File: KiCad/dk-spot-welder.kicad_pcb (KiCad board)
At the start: 4 copper layers, 112 x 72 mm, 49 parts, among them Q1 IRF1404, Q2 IRF1404, Q3 IRF1404, Q4 IRF1404, Q5 IRF1404, Q6 IRF1404, Q7 IRF1404, Q8 IRF1404, U1 MCP1407, U2 L7805, U3 ATtiny13-20P, U4 PC817

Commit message: added PCBWay logo
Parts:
- added G***: LOGO, LOGO, B.Cu at (107.5, 129.0)

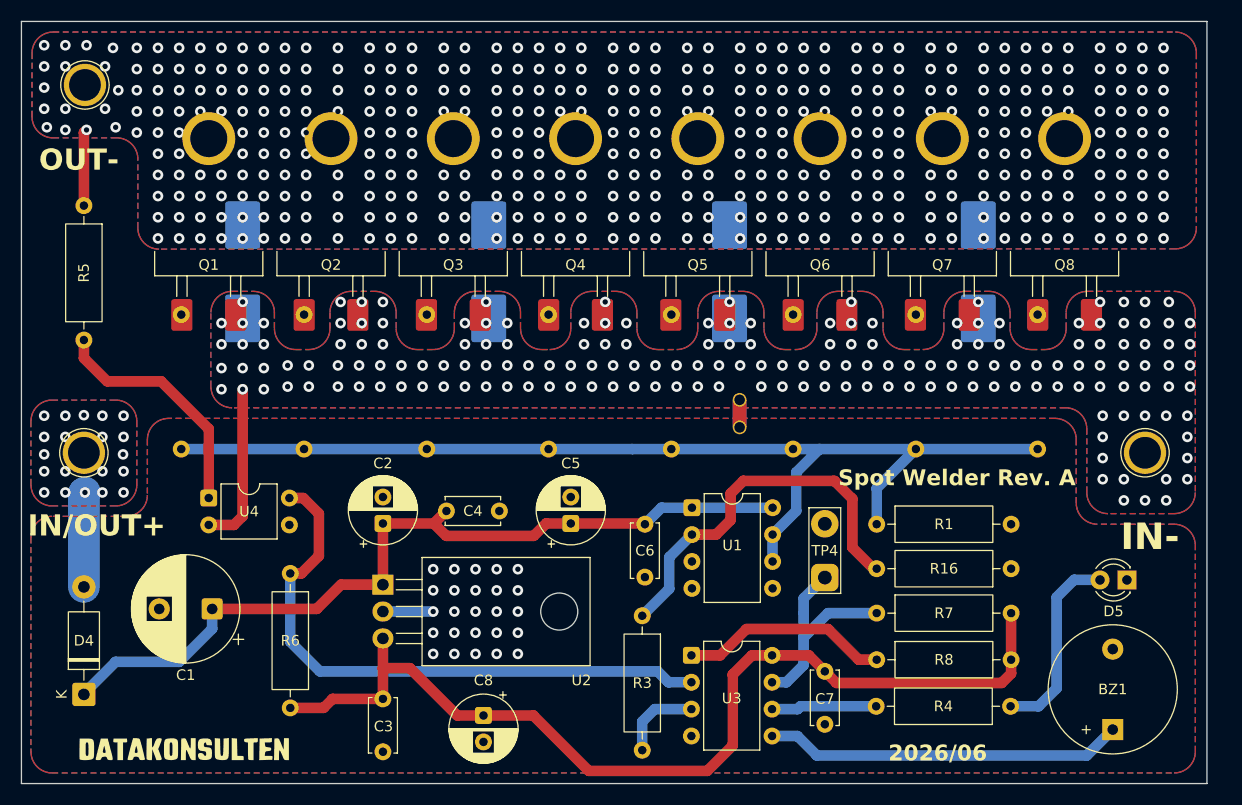
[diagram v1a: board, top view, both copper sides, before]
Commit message: update connections from M3 to 4mm
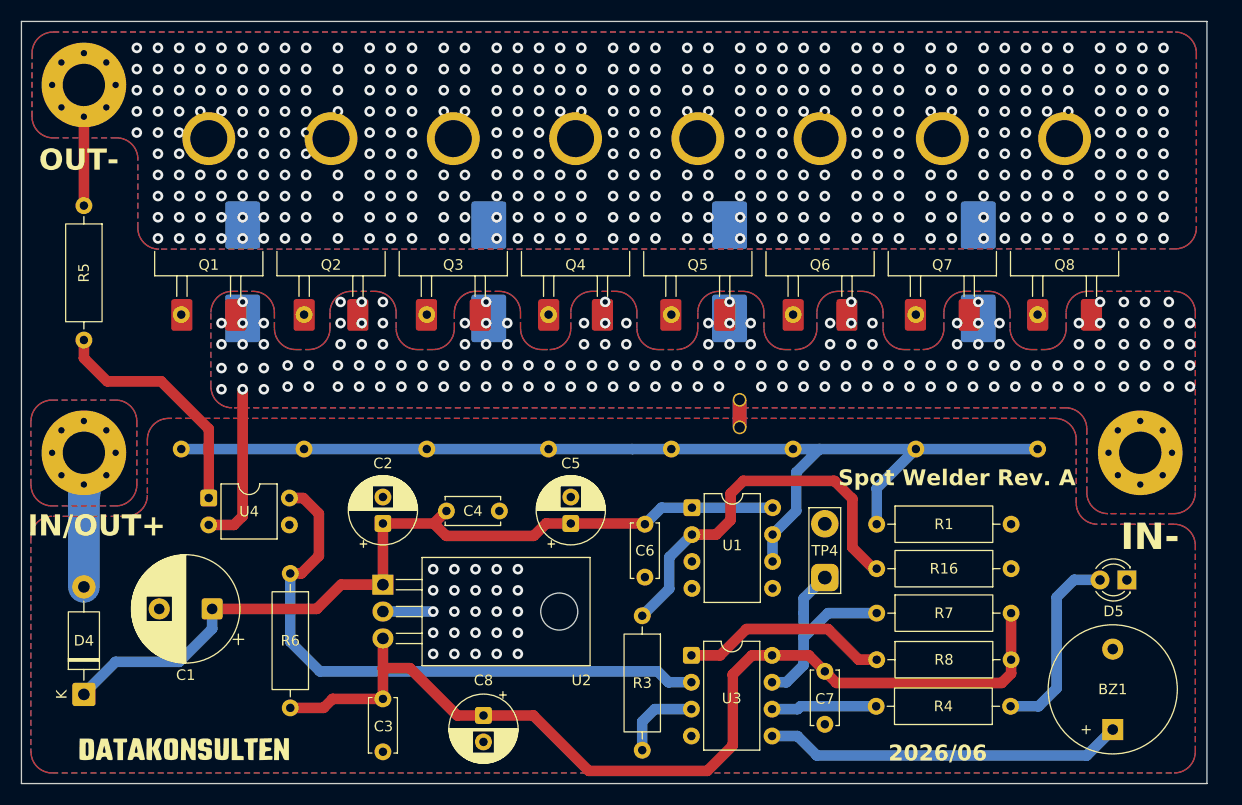
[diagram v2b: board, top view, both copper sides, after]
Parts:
- TP1, TP2, TP3: footprint TestPoint:TestPoint_Plated_Hole_D3.0mm -> MountingHole:MountingHole_4mm_Pad_Via
- moved TP1 0.45 mm to (197.8, 101.2)
- moved TP2 0.10 mm to (98.0, 66.5)
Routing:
- net /OUT-: track 7.25 -> 8.40 mm, vias 421 -> 405
- net GND: vias 174 -> 158
- net /IN/OUT+: vias 20 -> 0

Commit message: add another tp on PB5 to use with manual weld button
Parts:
- added TP5: WELD_BTN, TestPoint:TestPoint_2Pads_Pitch5.08mm_Drill1.3mm, F.Cu at (110.0, 124.8)
- TP4: value TestPoint_2Pole -> WELD_DURATION
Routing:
- net PB5: track 19.7 -> 69.1 mm, vias 0 -> 1
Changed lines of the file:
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@@
 			)
 		)
-		(property "Value" "TestPoint_2Pole"
+		(property "Value" "WELD_DURATION"
 			(at 2.54 3 90)
 			(layer "F.Fab")
@@
 		)
 	)
+	(footprint "TestPoint:TestPoint_2Pads_Pitch5.08mm_Drill1.3mm"
+		(layer "F.Cu")
+		(at 110 124.825 180)
+		(descr "Test point with 2 pads, pitch 5.08mm, hole diameter 1.3mm, wire diameter 1.0mm")
+		(tags "CONN DEV")
+		(property "Reference" "TP5"
+			(at 2.54 -2.5 0)
+			(layer "F.SilkS")
+			(effects
+				(font
+					(size 1 1)
+					(thickness 0.15)
+				)
+			)
+		)
+		(property "Value" "WELD_BTN"
+			(at 2.54 3 0)
+			(layer "F.Fab")
+			(effects
+				(font
+					(size 1 1)
+					(thickness 0.15)
+				)
+			)
+		)
+		(property "Datasheet" ""
+			(at 0 0 180)
+			(unlocked yes)
+			(layer "F.Fab")
+			(hide yes)
+			(effects
+				(font
+					(size 1.27 1.27)
+					(thickness 0.15)
+				)
+			)
+		)
+		(property "Description" "2-polar test point"
+			(at 0 0 180)
+			(unlocked yes)
+			(layer "F.Fab")
+			(hide yes)
+			(effects
+				(font
+					(size 1.27 1.27)
+					(thickness 0.15)
+				)
+			)
+		)
+		(property ki_fp_filters "Pin* Test*")
+		(sheetname "/")
+		(sheetfile "dk-spot-welder.kicad_sch")
+		(units
+			(unit
+				(name "A")
+				(pins "1" "2")
+			)
+		)
+		(duplicate_pad_numbers_are_jumpers no)
+		(fp_line
+			(start 6.6 1.5)
+			(end 6.6 -1.5)
+			(stroke
+				(width 0.12)
+				(type solid)
+			)
+			(layer "F.SilkS")
+		)
+		(fp_line
+			(start 6.6 1.5)
+			(end -1.5 1.5)
+			(stroke
+				(width 0.12)
+				(type solid)
+			)
+			(layer "F.SilkS")
+		)
+		(fp_line
+			(start -1.5 -1.5)
+			(end 6.6 -1.5)
+			(stroke
+				(width 0.12)
+				(type solid)
+			)
+			(layer "F.SilkS")
+		)
+		(fp_line
+			(start -1.5 -1.5)
+			(end -1.5 1.5)
+			(stroke
+				(width 0.12)
+				(type solid)
+			)
+			(layer "F.SilkS")
+		)
+		(fp_line
+			(start 6.88 1.8)
+			(end 6.88 -1.8)
+			(stroke
+				(width 0.05)
+				(type solid)
+			)
+			(layer "F.CrtYd")
+		)
+		(fp_line
+			(start 6.88 1.8)
+			(end -1.8 1.8)
+			(stroke
+				(width 0.05)
+				(type solid)
+			)
+			(layer "F.CrtYd")
+		)
+		(fp_line
+			(start -1.8 -1.8)
+			(end 6.88 -1.8)
+			(stroke
+				(width 0.05)
+				(type solid)
+			)
+			(layer "F.CrtYd")
+		)
+		(fp_line
+			(start -1.8 -1.8)
+			(end -1.8 1.8)
+			(stroke
+				(width 0.05)
+				(type solid)
+			)
+			(layer "F.CrtYd")
+		)
+		(fp_line
+			(start 5.08 0)
+			(end 0 0)
+			(stroke
+				(width 0.1)
+				(type solid)
+			)
+			(layer "F.Fab")
+		)
+		(fp_text user "${REFERENCE}"
+			(at 2.54 0 0)
+			(layer "F.Fab")
+			(effects
+				(font
+					(size 1 1)
+					(thickness 0.15)
+				)
+			)
+		)
+		(pad "1" thru_hole roundrect
+			(at 0 0 180)
+			(size 2.6 2.6)
+			(drill 1.3)
+			(layers "*.Cu" "*.Mask")
+			(remove_unused_layers no)
+			(roundrect_rratio 0.25)
+			(net "PB5")
+			(pinfunction "1_1")
+			(pintype "passive")
+		)
+		(pad "2" thru_hole circle
+			(at 5.08 0 180)
+			(size 2.6 2.6)
+			(drill 1.3)
+			(layers "*.Cu" "*.Mask")
+			(remove_unused_layers no)
+			(net "CTRL_GND")
+			(pinfunction "2_2")
+			(pintype "passive")
+		)
+		(embedded_fonts no)
+	)
 	(footprint "Capacitor_THT:C_Disc_D5.0mm_W2.5mm_P5.00mm"
 		(layer "F.Cu")
@@
 	)
 	(segment
+		(start 149.61 120.39)
+		(end 155.395 120.39)
+		(width 1)
+		(layer "F.Cu")
+		(net "PB5")
+	)
+	(segment
 		(start 172.9 120.8)
 		(end 171.2 120.8)
@@
 	)
 	(segment
+		(start 145 124)
+		(end 146 124)
+		(width 1)
+		(layer "F.Cu")
+		(net "PB5")
+	)
+	(segment
 		(start 171.2 120.8)
 		(end 168.3 117.9)
@@
 	)
 	(segment
+		(start 146 124)
+		(end 149.61 120.39)
+		(width 1)
+		(layer "F.Cu")
+		(net "PB5")
+	)
+	(segment
 		(start 158.11 120.39)
 		(end 155.395 120.39)
@@
 		(net "PB5")
 	)
+	(via
+		(at 145 124)
+		(size 0.6)
+		(drill 0.3)
+		(layers "F.Cu" "B.Cu")
+		(net "PB5")
+	)
+	(segment
+		(start 111.825 124.825)
+		(end 114.449781 127.449781)
+		(width 1)
+		(layer "B.Cu")
+		(net "PB5")
+	)
+	(segment
+		(start 132 124)
+		(end 145 124)
+		(width 1)
+		(layer "B.Cu")
+		(net "PB5")
+	)
+	(segment
+		(start 114.449781 127.449781)
+		(end 128.550219 127.449781)
+		(width 1)
+		(layer "B.Cu")
+		(net "PB5")
+	)
+	(segment
+		(start 128.550219 127.449781)
+		(end 132 124)
+		(width 1)
+		(layer "B.Cu")
+		(net "PB5")
+	)
+	(segment
+		(start 110 124.825)
+		(end 111.825 124.825)
+		(width 1)
+		(layer "B.Cu")
+		(net "PB5")
+	)
